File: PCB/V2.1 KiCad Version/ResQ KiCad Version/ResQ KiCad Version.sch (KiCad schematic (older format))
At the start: 7 parts, among them J1 Spare 1, J2 Spare 2, J3 OLED, J4 SD Card, J5 GPS, U1 WeMos_D1_mini

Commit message: KiCAD Project Updates
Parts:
- BT1: footprint (none) -> Connector_PinSocket_2.54mm:PinSocket_1x02_P2.54mm_Vertical
- J1, J2: footprint (none) -> Connector_PinSocket_2.54mm:PinSocket_1x03_P2.54mm_Vertical
- J3, J5: footprint (none) -> Connector_PinSocket_2.54mm:PinSocket_1x04_P2.54mm_Vertical
- J4: footprint (none) -> Connector_PinSocket_2.54mm:PinSocket_1x06_P2.54mm_Vertical
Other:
- note added: "NOTE: Some OLEDs Power & Ground are reversed"
- note removed: "NOTE: Some OLEDs VCC & GND are reversed"
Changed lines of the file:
@@
 F 0 "J3" H 8378 4326 50  0000 L CNN
 F 1 "OLED" H 8378 4235 50  0000 L CNN
-F 2 "" H 8350 4350 50  0001 C CNN
+F 2 "Connector_PinSocket_2.54mm:PinSocket_1x04_P2.54mm_Vertical" H 8350 4350 50  0001 C CNN
 F 3 "~" H 8350 4350 50  0001 C CNN
 	1    8350 4350
@@
 Wire Wire Line
 	5900 4200 5900 4250
-Text GLabel 6400 4100 1    50   Input ~ 0
-5V
 $Comp
 L MCU_Module:WeMos_D1_mini U1
@@
 F 0 "BT1" H 6258 4246 50  0000 L CNN
 F 1 "5V" H 6258 4155 50  0000 L CNN
-F 2 "" V 6150 4260 50  0001 C CNN
+F 2 "Connector_PinSocket_2.54mm:PinSocket_1x02_P2.54mm_Vertical" V 6150 4260 50  0001 C CNN
 F 3 "~" V 6150 4260 50  0001 C CNN
 	1    6150 4200
@@
 F 0 "J1" H 6128 5076 50  0000 L CNN
 F 1 "Spare 1" H 6128 4985 50  0000 L CNN
-F 2 "" H 6100 5050 50  0001 C CNN
+F 2 "Connector_PinSocket_2.54mm:PinSocket_1x03_P2.54mm_Vertical" H 6100 5050 50  0001 C CNN
 F 3 "~" H 6100 5050 50  0001 C CNN
 	1    6100 5050
@@
 F 0 "J2" H 6128 5426 50  0000 L CNN
 F 1 "Spare 2" H 6128 5335 50  0000 L CNN
-F 2 "" H 6100 5400 50  0001 C CNN
+F 2 "Connector_PinSocket_2.54mm:PinSocket_1x03_P2.54mm_Vertical" H 6100 5400 50  0001 C CNN
 F 3 "~" H 6100 5400 50  0001 C CNN
 	1    6100 5400
@@
 F 0 "J5" H 8378 5826 50  0000 L CNN
 F 1 "GPS" H 8378 5735 50  0000 L CNN
-F 2 "" H 8350 5850 50  0001 C CNN
+F 2 "Connector_PinSocket_2.54mm:PinSocket_1x04_P2.54mm_Vertical" H 8350 5850 50  0001 C CNN
 F 3 "~" H 8350 5850 50  0001 C CNN
 	1    8350 5850
@@
 L power:GND #PWR02
 U 1 1 5F34FDAC
-P 7150 5800
-F 0 "#PWR02" H 7150 5550 50  0001 C CNN
-F 1 "GND" H 7155 5627 50  0000 C CNN
-F 2 "" H 7150 5800 50  0001 C CNN
-F 3 "" H 7150 5800 50  0001 C CNN
-	1    7150 5800
+P 7150 5900
+F 0 "#PWR02" H 7150 5650 50  0001 C CNN
+F 1 "GND" H 7155 5727 50  0000 C CNN
+F 2 "" H 7150 5900 50  0001 C CNN
+F 3 "" H 7150 5900 50  0001 C CNN
+	1    7150 5900
 	1    0    0    -1
 $EndComp
@@
 F 0 "J4" H 8378 5076 50  0000 L CNN
 F 1 "SD Card" H 8378 4985 50  0000 L CNN
-F 2 "" H 8350 5100 50  0001 C CNN
+F 2 "Connector_PinSocket_2.54mm:PinSocket_1x06_P2.54mm_Vertical" H 8350 5100 50  0001 C CNN
 F 3 "~" H 8350 5100 50  0001 C CNN
 	1    8350 5100
@@
 $EndComp
 Text Notes 7900 4050 0    50   ~ 0
-NOTE: Some OLEDs VCC & GND are reversed
+NOTE: Some OLEDs Power & Ground are reversed
 $Bitmap
-Pos 6150 6550
-Scale 0.250000
+Pos 6050 6900
+Scale 0.350000
 Data
 89 50 4E 47 0D 0A 1A 0A 00 00 00 0D 49 48 44 52 00 00 04 B0 00 00 04 EF 08 06 00 00 00 16 F9 09
@@
 EndData
 $EndBitmap
+Wire Wire Line
+	7150 5800 7150 5900
+Text GLabel 6400 4100 1    50   Input ~ 0
+5V
 $EndSCHEMATC

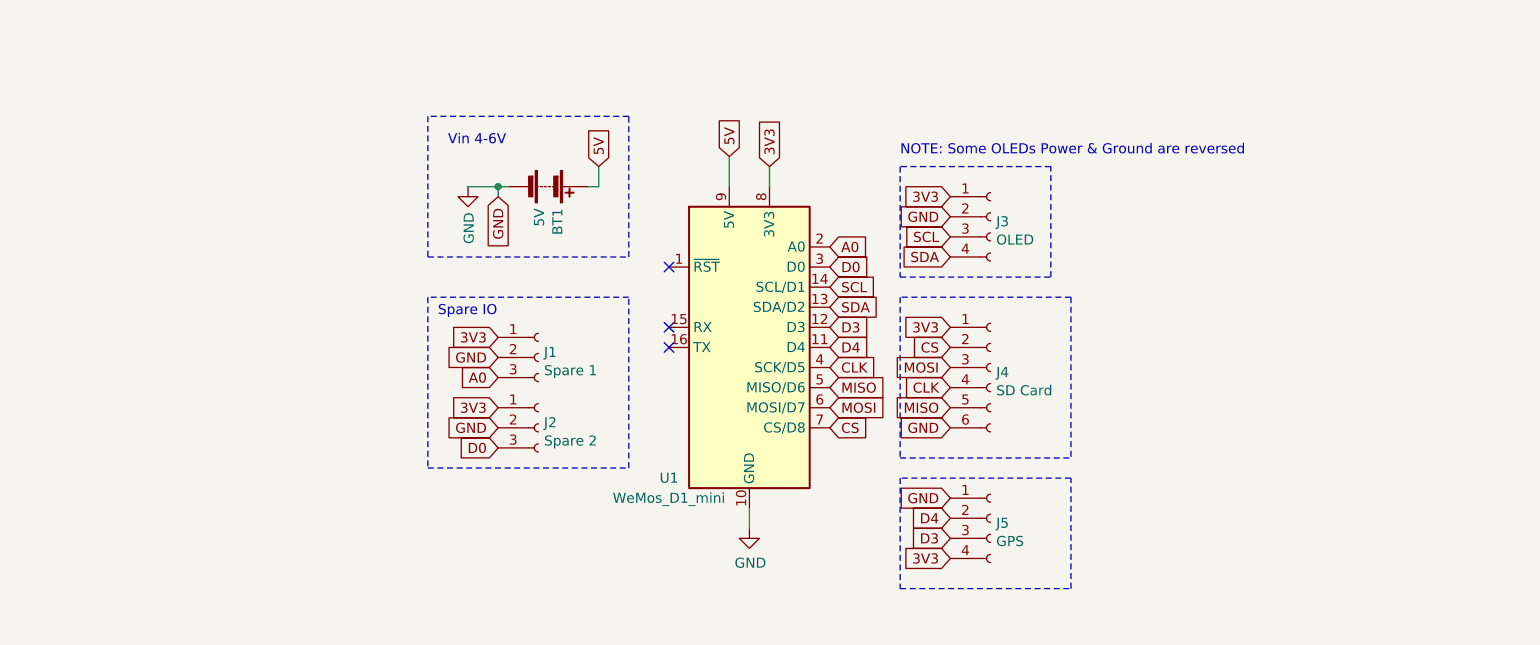
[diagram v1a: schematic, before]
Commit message: oled pinout reversal
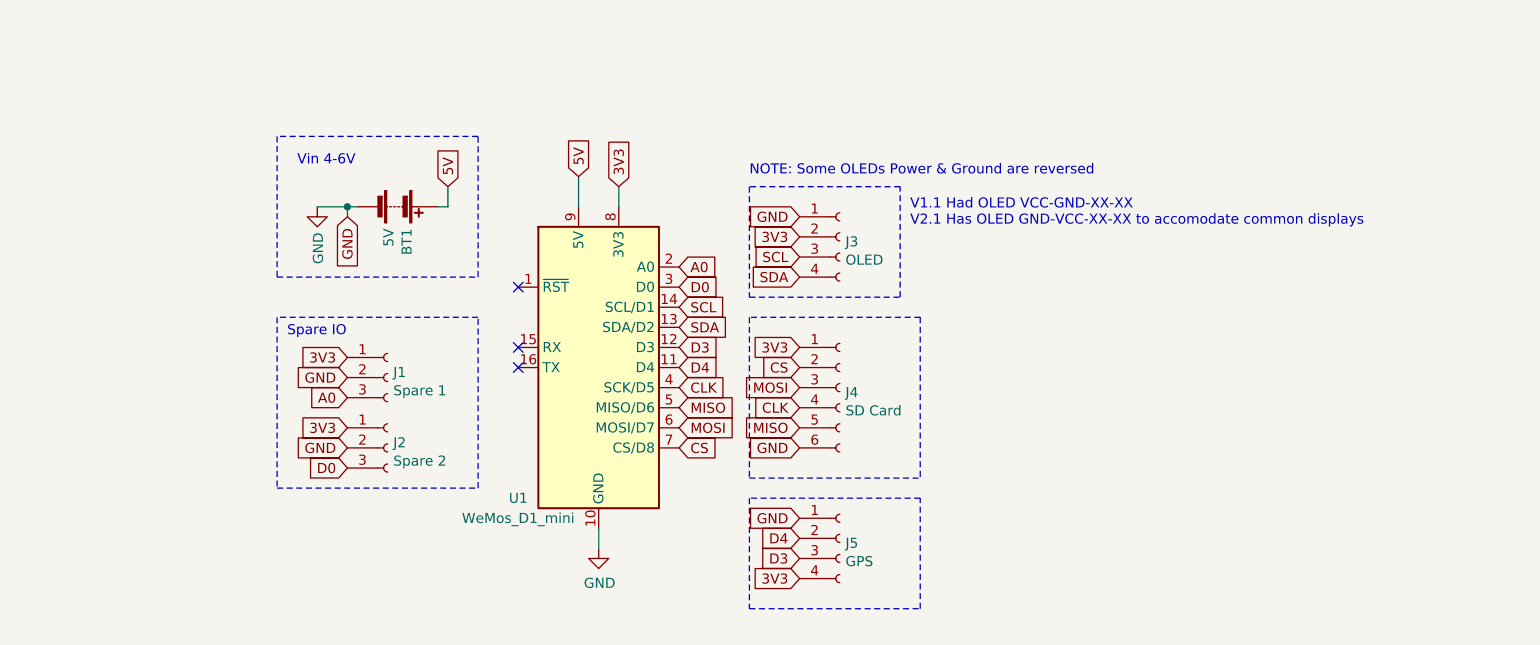
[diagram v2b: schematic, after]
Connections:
- net 3V3: now also J3.2 (Pin_2); no longer J3.1 (Pin_1)
- net GND: now also J3.1 (Pin_1); no longer J3.2 (Pin_2)
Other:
- note added: "V1.1 Had OLED VCC-GND-XX-XX\nV2.1 Has OLED GND-VCC-XX-XX to accomodate common displays\n"
- moved on the sheet: BT1, J1, J2, J3, J4, J5, U1

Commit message: Purdier schematic
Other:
- note added: "GPS Receiver"
- note added: "Microcontroller"
- note added: "OLED Display"
- note added: "Power Management"
- note added: "SPI SD Card"
- note added: "V1.1 Had OLED VCC-GND-XX-XX\nV2.1 Has OLED GND-VCC-XX-XX \n"
- note removed: "V1.1 Had OLED VCC-GND-XX-XX\nV2.1 Has OLED GND-VCC-XX-XX to accomodate common displays\n"
- moved on the sheet: BT1, J1, J2, J3, J4, J5, U1

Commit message: Purdy schematico
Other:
- moved on the sheet: BT1, J1, J2, J3, J4, J5, U1

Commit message: schem
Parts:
- added R1: 10k, Resistor_SMD:R_0201_0603Metric, symbol Device:R
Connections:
- net 3V3: now also R1.1
- net MISO: now also R1.2
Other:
- note added: "10K pullup"
- note added: "Note:\nBN220 has no compass but has battery for \nquick signal lock if location hasn't moved."
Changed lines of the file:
@@
 Wire Notes Line
 	5550 5950 7450 5950
+$Comp
+L Device:R R1
+U 1 1 5F3B9579
+P 8750 5050
+F 0 "R1" H 8820 5096 50  0000 L CNN
+F 1 "10k" H 8820 5005 50  0000 L CNN
+F 2 "Resistor_SMD:R_0201_0603Metric" V 8680 5050 50  0001 C CNN
+F 3 "~" H 8750 5050 50  0001 C CNN
+	1    8750 5050
+	1    0    0    -1
+$EndComp
+Text GLabel 8750 4850 1    50   Input ~ 0
+3V3
+Text GLabel 8750 5250 3    50   Input ~ 0
+MISO
+Wire Wire Line
+	8750 4850 8750 4900
+Wire Wire Line
+	8750 5200 8750 5250
+Text Notes 9000 5050 0    50   ~ 0
+10K pullup
+Text Notes 8400 6050 0    50   ~ 0
+Note:\nBN220 has no compass but has battery for \nquick signal lock if location hasn't moved.
 $EndSCHEMATC

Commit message: Schematic purrdy
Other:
- note added: "Note:\n10K pullup not always needed \nbut without can cause random \nwrite errors"
- note removed: "10K pullup"
- moved on the sheet: BT1, J1, J2, J3, J4, J5, R1, U1

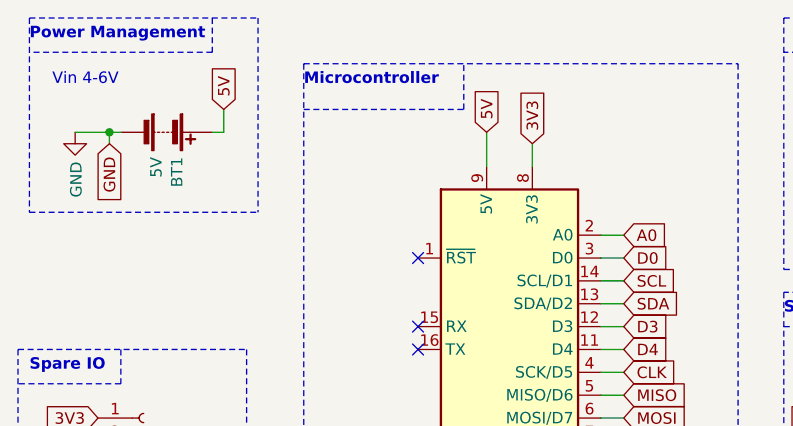
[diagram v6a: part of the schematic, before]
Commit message: Schematic Updates
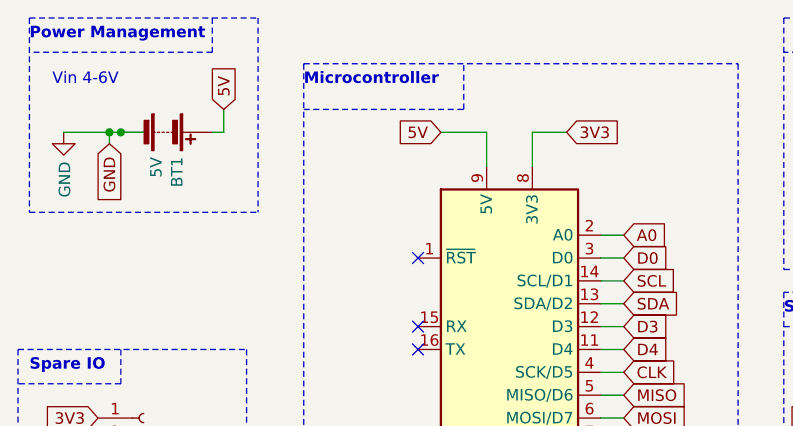
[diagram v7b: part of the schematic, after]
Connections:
- wire segments 20 -> 23
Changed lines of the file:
@@
 Wire Notes Line
 	4900 4200 5900 4200
-Wire Wire Line
-	5100 3850 5250 3850
-Connection ~ 5250 3850
-Wire Wire Line
-	5750 3850 5700 3850
-Wire Wire Line
-	5750 3750 5750 3850
 Text Notes 5000 3650 0    50   ~ 0
 Vin 4-6V
-Wire Wire Line
-	5250 3850 5250 3900
-Text GLabel 6900 3850 1    50   Input ~ 0
+Text GLabel 6700 3850 0    50   Input ~ 0
 5V
+Text GLabel 5200 5300 0    50   Input ~ 0
+A0
+Text GLabel 5200 5200 0    50   Input ~ 0
+GND
+Text GLabel 5200 5100 0    50   Input ~ 0
+3V3
+NoConn ~ 6600 4800
+NoConn ~ 6600 4700
+NoConn ~ 6600 4400
+Text GLabel 7500 4700 2    50   Input ~ 0
+D3
+Text GLabel 7500 4800 2    50   Input ~ 0
+D4
+Text GLabel 8500 6000 0    50   Input ~ 0
+GND
+Text GLabel 7250 3850 2    50   Input ~ 0
+3V3
+Text GLabel 7500 4900 2    50   Input ~ 0
+CLK
+Text GLabel 7500 5000 2    50   Input ~ 0
+MISO
+Text GLabel 7500 5100 2    50   Input ~ 0
+MOSI
+Text GLabel 7500 5200 2    50   Input ~ 0
+CS
+Text GLabel 8500 5400 0    50   Input ~ 0
+GND
+Text GLabel 8500 4900 0    50   Input ~ 0
+3V3
+Text GLabel 8500 5200 0    50   Input ~ 0
+CLK
+Text GLabel 8500 5300 0    50   Input ~ 0
+MISO
+Text GLabel 8500 5100 0    50   Input ~ 0
+MOSI
+Text GLabel 8500 5000 0    50   Input ~ 0
+CS
+$Comp
+L Connector:Conn_01x06_Female J4
+U 1 1 5F31DE3A
+P 8700 5100
+F 0 "J4" H 8728 5076 50  0000 L CNN
+F 1 "SD Card" H 8728 4985 50  0000 L CNN
+F 2 "Connector_PinSocket_2.54mm:PinSocket_1x06_P2.54mm_Vertical" H 8700 5100 50  0001 C CNN
+F 3 "~" H 8700 5100 50  0001 C CNN
+	1    8700 5100
+	1    0    0    -1
+$EndComp
+Wire Wire Line
+	7000 5600 7000 5700
+Text GLabel 8500 4050 0    50   Input ~ 0
+3V3
+Text Notes 8250 3750 0    50   ~ 0
+NOTE: Some OLEDs Power & Ground are reversed
+Text Notes 9050 4000 0    50   ~ 0
+V1.1 Had OLED VCC-GND-XX-XX\nV2.1 Has OLED GND-VCC-XX-XX \n
+Text GLabel 8500 6300 0    50   Input ~ 0
+3V3
+$Comp
+L power:GND #PWR02
+U 1 1 5F34FDAC
+P 7000 5700
+F 0 "#PWR02" H 7000 5450 50  0001 C CNN
+F 1 "GND" H 7005 5527 50  0000 C CNN
+F 2 "" H 7000 5700 50  0001 C CNN
+F 3 "" H 7000 5700 50  0001 C CNN
+	1    7000 5700
+	1    0    0    -1
+$EndComp
+Wire Notes Line
+	10700 3350 10700 4450
+Wire Notes Line
+	8200 3350 10700 3350
+Wire Notes Line
+	8200 4450 10700 4450
+Wire Notes Line
+	8000 3550 8000 5950
+Wire Notes Line
+	6100 3550 8000 3550
+Wire Notes Line
+	6100 5950 8000 5950
+$Comp
+L Device:R R1
+U 1 1 5F3B9579
+P 9200 5050
+F 0 "R1" H 9270 5096 50  0000 L CNN
+F 1 "10k" H 9270 5005 50  0000 L CNN
+F 2 "Resistor_SMD:R_0201_0603Metric" V 9130 5050 50  0001 C CNN
+F 3 "~" H 9200 5050 50  0001 C CNN
+	1    9200 5050
+	1    0    0    -1
+$EndComp
+Text GLabel 9200 4850 1    50   Input ~ 0
+3V3
+Text GLabel 9200 5250 3    50   Input ~ 0
+MISO
+Wire Wire Line
+	9200 4850 9200 4900
+Wire Wire Line
+	9200 5200 9200 5250
+Text Notes 8950 6050 0    50   ~ 0
+Note:\nBN220 has no compass but has battery for \nquick signal lock if location hasn't moved.
+$Comp
+L MCU_Module:WeMos_D1_mini U1
+U 1 1 5F31691B
+P 7000 4800
+F 0 "U1" H 6250 3850 50  0000 C CNN
+F 1 "WeMos_D1_mini" H 6500 3750 50  0000 C CNN
+F 2 "Module:WEMOS_D1_mini_light" H 7000 3650 50  0001 C CNN
+F 3 "https://wiki.wemos.cc/products:d1:d1_mini#documentation" H 5150 3650 50  0001 C CNN
+	1    7000 4800
+	1    0    0    -1
+$EndComp
+Text GLabel 5200 5550 0    50   Input ~ 0
+3V3
+$Comp
+L Connector:Conn_01x03_Female J1
+U 1 1 5F3230C4
+P 5400 5200
+F 0 "J1" H 5428 5226 50  0000 L CNN
+F 1 "Spare 1" H 5428 5135 50  0000 L CNN
+F 2 "Connector_PinSocket_2.54mm:PinSocket_1x03_P2.54mm_Vertical" H 5400 5200 50  0001 C CNN
+F 3 "~" H 5400 5200 50  0001 C CNN
+	1    5400 5200
+	1    0    0    -1
+$EndComp
+Text GLabel 5200 5650 0    50   Input ~ 0
+GND
+Text GLabel 5200 5750 0    50   Input ~ 0
+D0
+$Comp
+L Connector:Conn_01x03_Female J2
+U 1 1 5F322635
+P 5400 5650
+F 0 "J2" H 5428 5676 50  0000 L CNN
+F 1 "Spare 2" H 5428 5585 50  0000 L CNN
+F 2 "Connector_PinSocket_2.54mm:PinSocket_1x03_P2.54mm_Vertical" H 5400 5650 50  0001 C CNN
+F 3 "~" H 5400 5650 50  0001 C CNN
+	1    5400 5650
+	1    0    0    -1
+$EndComp
+Wire Notes Line
+	4850 6000 5850 6000
+Wire Notes Line
+	4850 4800 4850 6000
+Wire Notes Line
+	5850 4800 5850 6000
+Text Notes 9450 4900 0    50   ~ 0
+Note:\n10K pullup not always needed \nbut without can cause random \nwrite errors
+Text GLabel 5750 3750 1    50   Input ~ 0
+5V
+Text GLabel 5250 3900 3    50   Input ~ 0
+GND
+$Comp
+L power:GND #PWR01
+U 1 1 5F34EF30
+P 5050 3850
+F 0 "#PWR01" H 5050 3600 50  0001 C CNN
+F 1 "GND" V 5055 3722 50  0000 R CNN
+F 2 "" H 5050 3850 50  0001 C CNN
+F 3 "" H 5050 3850 50  0001 C CNN
+	1    5050 3850
+	1    0    0    -1
+$EndComp
 $Comp
 L Device:Battery BT1
@@
 	0    1    1    0
 $EndComp
-$Comp
-L power:GND #PWR01
-U 1 1 5F34EF30
-P 5100 3850
-F 0 "#PWR01" H 5100 3600 50  0001 C CNN
-F 1 "GND" V 5105 3722 50  0000 R CNN
-F 2 "" H 5100 3850 50  0001 C CNN
-F 3 "" H 5100 3850 50  0001 C CNN
-	1    5100 3850
-	1    0    0    -1
-$EndComp
-Text GLabel 5250 3900 3    50   Input ~ 0
-GND
-Wire Wire Line
-	5300 3850 5250 3850
-Text GLabel 5200 5300 0    50   Input ~ 0
-A0
-Text GLabel 5200 5200 0    50   Input ~ 0
-GND
-Text GLabel 5200 5100 0    50   Input ~ 0
-3V3
-Wire Wire Line
-	7100 3900 7100 4000
-NoConn ~ 6600 4800
-NoConn ~ 6600 4700
-NoConn ~ 6600 4400
-Text GLabel 7500 4700 2    50   Input ~ 0
-D3
-Text GLabel 7500 4800 2    50   Input ~ 0
-D4
-Text GLabel 8500 6000 0    50   Input ~ 0
-GND
-Text GLabel 7100 3900 1    50   Input ~ 0
-3V3
-Text GLabel 7500 4900 2    50   Input ~ 0
-CLK
-Text GLabel 7500 5000 2    50   Input ~ 0
-MISO
-Text GLabel 7500 5100 2    50   Input ~ 0
-MOSI
-Text GLabel 7500 5200 2    50   Input ~ 0
-CS
-Text GLabel 8500 5400 0    50   Input ~ 0
-GND
-Text GLabel 8500 4900 0    50   Input ~ 0
-3V3
-Text GLabel 8500 5200 0    50   Input ~ 0
-CLK
-Text GLabel 8500 5300 0    50   Input ~ 0
-MISO
-Text GLabel 8500 5100 0    50   Input ~ 0
-MOSI
-Text GLabel 8500 5000 0    50   Input ~ 0
-CS
-$Comp
-L Connector:Conn_01x06_Female J4
-U 1 1 5F31DE3A
-P 8700 5100
-F 0 "J4" H 8728 5076 50  0000 L CNN
-F 1 "SD Card" H 8728 4985 50  0000 L CNN
-F 2 "Connector_PinSocket_2.54mm:PinSocket_1x06_P2.54mm_Vertical" H 8700 5100 50  0001 C CNN
-F 3 "~" H 8700 5100 50  0001 C CNN
-	1    8700 5100
-	1    0    0    -1
-$EndComp
-Wire Wire Line
-	7000 5600 7000 5700
-Text GLabel 5750 3750 1    50   Input ~ 0
-5V
-Text GLabel 8500 4050 0    50   Input ~ 0
-3V3
-Text Notes 8250 3750 0    50   ~ 0
-NOTE: Some OLEDs Power & Ground are reversed
-Text Notes 9050 4000 0    50   ~ 0
-V1.1 Had OLED VCC-GND-XX-XX\nV2.1 Has OLED GND-VCC-XX-XX \n
-Text GLabel 8500 6300 0    50   Input ~ 0
-3V3
-$Comp
-L power:GND #PWR02
-U 1 1 5F34FDAC
-P 7000 5700
-F 0 "#PWR02" H 7000 5450 50  0001 C CNN
-F 1 "GND" H 7005 5527 50  0000 C CNN
-F 2 "" H 7000 5700 50  0001 C CNN
-F 3 "" H 7000 5700 50  0001 C CNN
-	1    7000 5700
-	1    0    0    -1
-$EndComp
-Wire Notes Line
-	10700 3350 10700 4450
-Wire Notes Line
-	8200 3350 10700 3350
-Wire Notes Line
-	8200 4450 10700 4450
-Wire Notes Line
-	8000 3550 8000 5950
-Wire Notes Line
-	6100 3550 8000 3550
-Wire Notes Line
-	6100 5950 8000 5950
-$Comp
-L Device:R R1
-U 1 1 5F3B9579
-P 9200 5050
-F 0 "R1" H 9270 5096 50  0000 L CNN
-F 1 "10k" H 9270 5005 50  0000 L CNN
-F 2 "Resistor_SMD:R_0201_0603Metric" V 9130 5050 50  0001 C CNN
-F 3 "~" H 9200 5050 50  0001 C CNN
-	1    9200 5050
-	1    0    0    -1
-$EndComp
-Text GLabel 9200 4850 1    50   Input ~ 0
-3V3
-Text GLabel 9200 5250 3    50   Input ~ 0
-MISO
-Wire Wire Line
-	9200 4850 9200 4900
-Wire Wire Line
-	9200 5200 9200 5250
-Text Notes 8950 6050 0    50   ~ 0
-Note:\nBN220 has no compass but has battery for \nquick signal lock if location hasn't moved.
-$Comp
-L MCU_Module:WeMos_D1_mini U1
-U 1 1 5F31691B
-P 7000 4800
-F 0 "U1" H 6250 3850 50  0000 C CNN
-F 1 "WeMos_D1_mini" H 6500 3750 50  0000 C CNN
-F 2 "Module:WEMOS_D1_mini_light" H 7000 3650 50  0001 C CNN
-F 3 "https://wiki.wemos.cc/products:d1:d1_mini#documentation" H 5150 3650 50  0001 C CNN
-	1    7000 4800
-	1    0    0    -1
-$EndComp
-Text GLabel 5200 5550 0    50   Input ~ 0
-3V3
-$Comp
-L Connector:Conn_01x03_Female J1
-U 1 1 5F3230C4
-P 5400 5200
-F 0 "J1" H 5428 5226 50  0000 L CNN
-F 1 "Spare 1" H 5428 5135 50  0000 L CNN
-F 2 "Connector_PinSocket_2.54mm:PinSocket_1x03_P2.54mm_Vertical" H 5400 5200 50  0001 C CNN
-F 3 "~" H 5400 5200 50  0001 C CNN
-	1    5400 5200
-	1    0    0    -1
-$EndComp
-Text GLabel 5200 5650 0    50   Input ~ 0
-GND
-Text GLabel 5200 5750 0    50   Input ~ 0
-D0
-$Comp
-L Connector:Conn_01x03_Female J2
-U 1 1 5F322635
-P 5400 5650
-F 0 "J2" H 5428 5676 50  0000 L CNN
-F 1 "Spare 2" H 5428 5585 50  0000 L CNN
-F 2 "Connector_PinSocket_2.54mm:PinSocket_1x03_P2.54mm_Vertical" H 5400 5650 50  0001 C CNN
-F 3 "~" H 5400 5650 50  0001 C CNN
-	1    5400 5650
-	1    0    0    -1
-$EndComp
-Wire Notes Line
-	4850 6000 5850 6000
-Wire Notes Line
-	4850 4800 4850 6000
-Wire Notes Line
-	5850 4800 5850 6000
-Text Notes 9450 4900 0    50   ~ 0
-Note:\n10K pullup not always needed \nbut without can cause random \nwrite errors
+Wire Wire Line
+	5250 3850 5250 3900
+Wire Wire Line
+	5750 3750 5750 3850
+Wire Wire Line
+	5750 3850 5700 3850
+Wire Wire Line
+	5050 3850 5250 3850
+Connection ~ 5250 3850
+Wire Wire Line
+	5250 3850 5300 3850
+Connection ~ 5300 3850
+Wire Wire Line
+	5300 3850 5400 3850
+Wire Wire Line
+	7100 3850 7100 4000
+Wire Wire Line
+	6700 3850 6900 3850
+Wire Wire Line
+	7100 3850 7250 3850
 $EndSCHEMATC

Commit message: v
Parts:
- renumbered BT1 to B1
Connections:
- wire segments 23 -> 22
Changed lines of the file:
@@
 Sheet 1 1
 Title "ResQ Open Source Search and Rescue Hardware"
-Date "2020-08-10"
+Date "2020-08-17"
 Rev "2.1"
 Comp "MKME Lab"
@@
 	4850 4800 5850 4800
 Wire Notes Line
-	5700 3500 4900 3500
-Wire Notes Line
-	5700 3350 5700 3500
-Wire Notes Line
-	4900 3350 4900 4200
-Wire Notes Line
-	5900 3350 5900 4200
-Wire Notes Line
-	4900 3350 5900 3350
+	5750 3500 4950 3500
+Wire Notes Line
+	5750 3350 5750 3500
+Wire Notes Line
+	4950 3350 4950 4200
+Wire Notes Line
+	5950 3350 5950 4200
+Wire Notes Line
+	4950 3350 5950 3350
 Wire Notes Line
 	6100 3550 6100 5950
@@
 Wire Notes Line
 	8200 3350 8200 4450
-Text Notes 4900 3450 0    50   ~ 10
+Text Notes 4950 3450 0    50   ~ 10
 Power Management
 Text Notes 6100 3650 0    50   ~ 10
@@
 SDA
 Wire Notes Line
-	4900 4200 5900 4200
-Text Notes 5000 3650 0    50   ~ 0
+	4950 4200 5950 4200
+Text Notes 5000 3600 0    50   ~ 0
 Vin 4-6V
 Text GLabel 6700 3850 0    50   Input ~ 0
@@
 Text Notes 9450 4900 0    50   ~ 0
 Note:\n10K pullup not always needed \nbut without can cause random \nwrite errors
-Text GLabel 5750 3750 1    50   Input ~ 0
+Text GLabel 5750 3850 2    50   Input ~ 0
 5V
 Text GLabel 5250 3900 3    50   Input ~ 0
@@
 $EndComp
 $Comp
-L Device:Battery BT1
+L Device:Battery B1
 U 1 1 5F31A8A9
 P 5500 3850
-F 0 "BT1" H 5608 3896 50  0000 L CNN
-F 1 "5V" H 5608 3805 50  0000 L CNN
+F 0 "B1" V 5650 3800 50  0000 L CNN
+F 1 "5V" V 5350 3800 50  0000 L CNN
 F 2 "Connector_PinSocket_2.54mm:PinSocket_1x02_P2.54mm_Vertical" V 5500 3910 50  0001 C CNN
 F 3 "~" V 5500 3910 50  0001 C CNN
@@
 	5250 3850 5250 3900
 Wire Wire Line
-	5750 3750 5750 3850
-Wire Wire Line
 	5750 3850 5700 3850
